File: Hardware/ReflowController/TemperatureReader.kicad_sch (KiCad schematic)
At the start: 12 parts, among them U4 MAX31865xAP

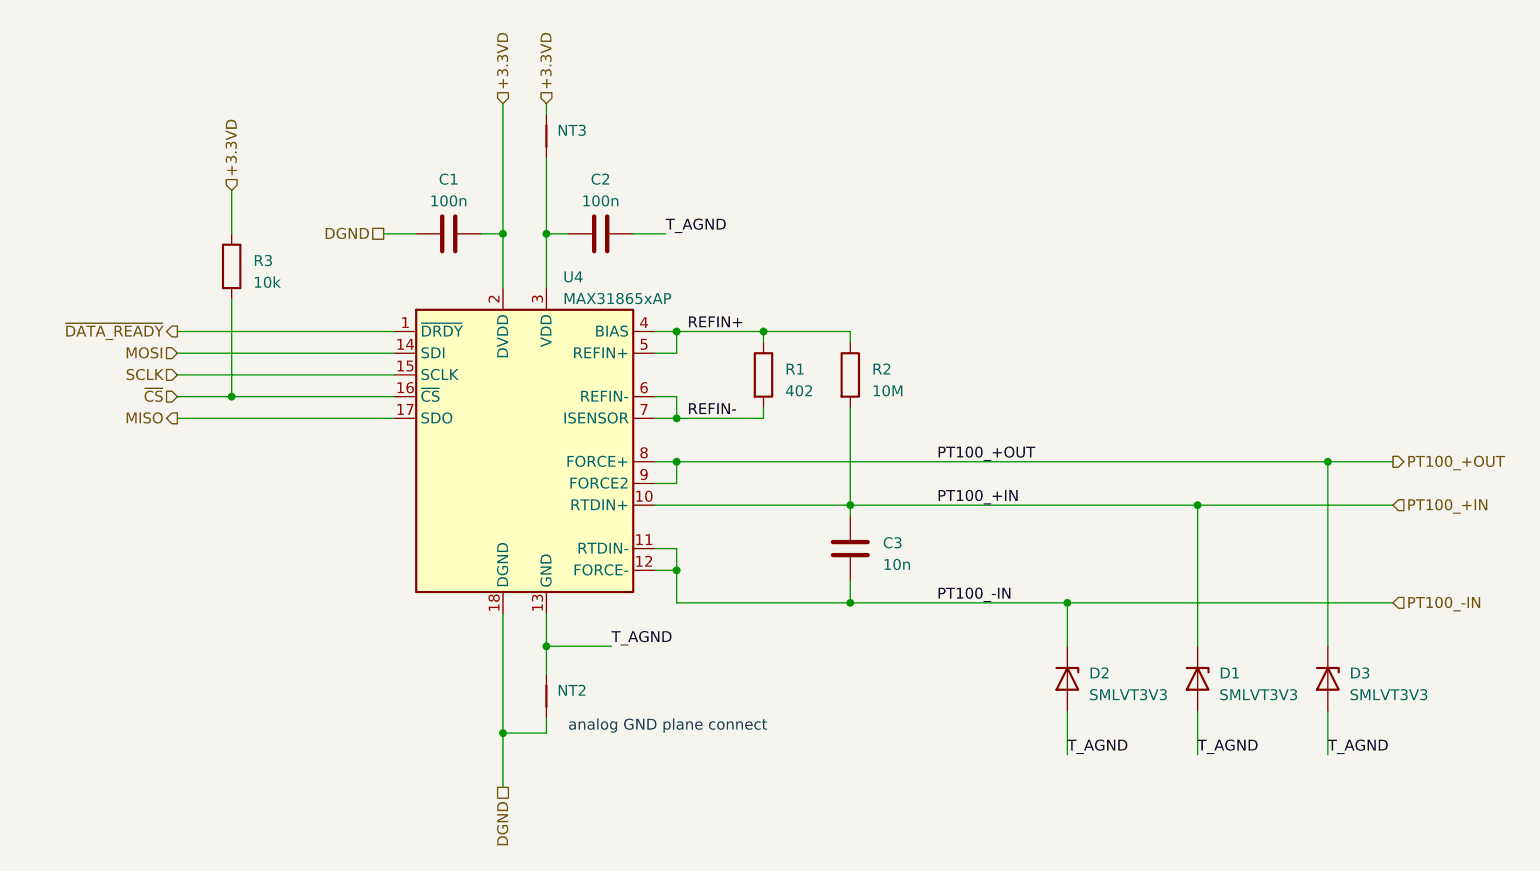
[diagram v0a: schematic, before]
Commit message: added the schematic of the updated pwerAndUi branch(with uC schematic update
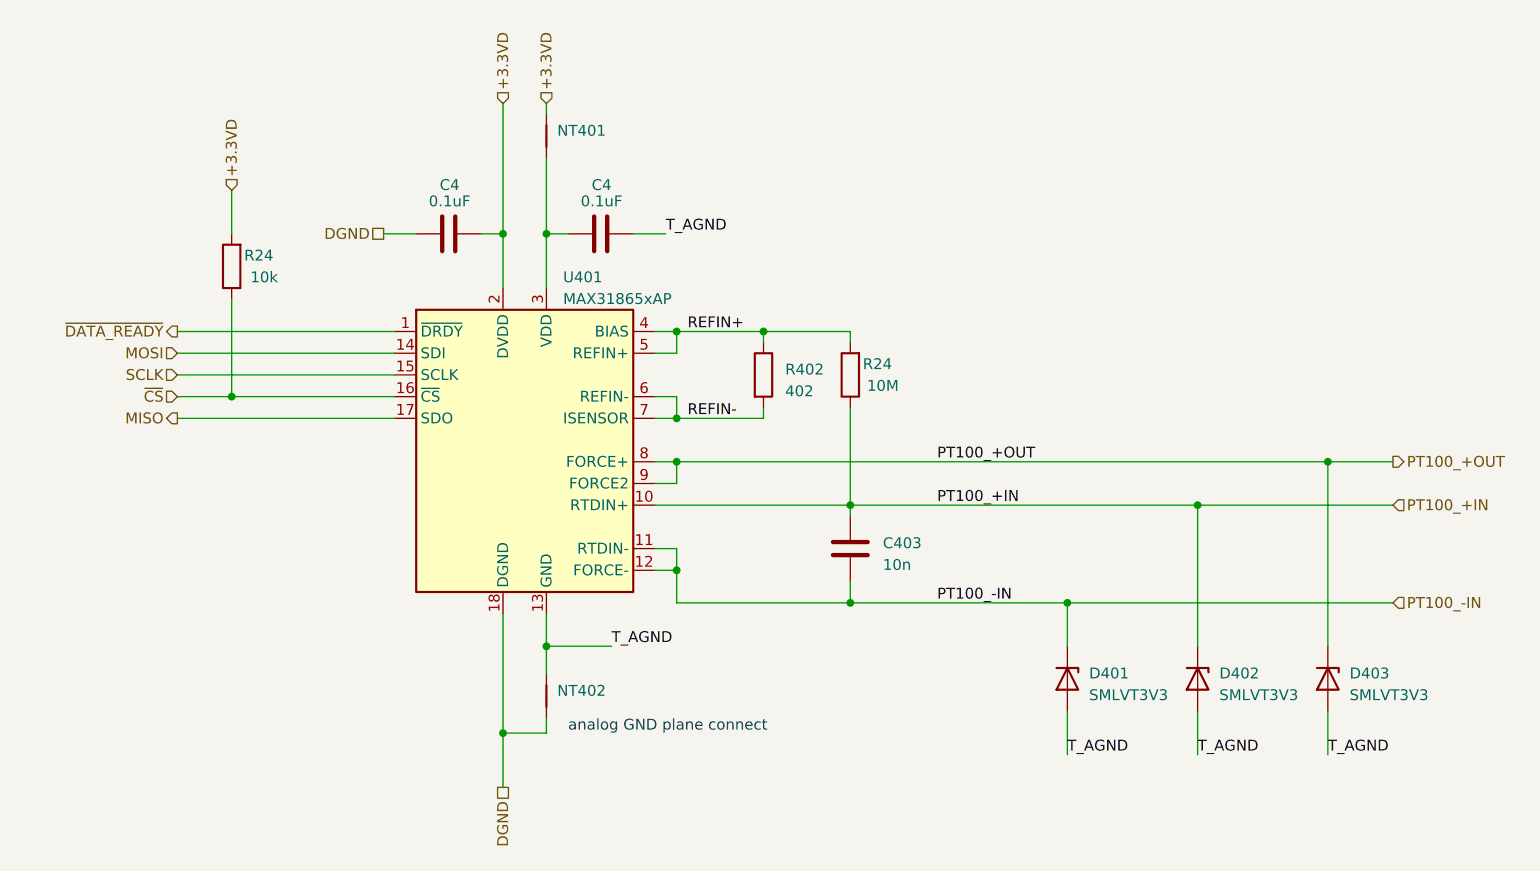
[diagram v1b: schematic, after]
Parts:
- removed C1, C2: 100n, Capacitor_SMD:C_1206_3216Metric, symbol Device:C
- removed D1, D3: SMLVT3V3, symbol Device:D_Zener
- removed R2: 10M, Resistor_SMD:R_1206_3216Metric, symbol Device:R
- removed R3: 10k, Resistor_SMD:R_1206_3216Metric, symbol Device:R
- added C4 (x2): 0.1uF, Capacitor_SMD:C_1206_3216Metric, symbol Device:C
- added D402, D403: SMLVT3V3, Diode_SMD:D_SMB_Handsoldering, symbol Device:D_Zener
- added R24: 10M, Resistor_SMD:R_0603_1608Metric_Pad0.98x0.95mm_HandSolder, symbol Device:R
- added R24: 10k, Resistor_SMD:R_0603_1608Metric_Pad0.98x0.95mm_HandSolder, symbol Device:R
- C403: renamed from C3; Field8 (none) -> 490-1754-2-ND; disti (none) -> digikey; man (none) -> murata; man_no (none) -> GRM3195C1H103JA01D
- D401: renamed from D2; footprint (none) -> Diode_SMD:D_SMB_Handsoldering; disti (none) -> digikey; disti_no (none) -> 497-2496-2-ND; man (none) -> stm; man_no (none) -> SMLVT3V3
- NT401: renamed from NT3; footprint (none) -> NetTie:NetTie-2_SMD_Pad0.5mm
- NT402: renamed from NT2; footprint (none) -> NetTie:NetTie-2_SMD_Pad0.5mm
- R402: renamed from R1; footprint (none) -> Resistor_SMD:R_1206_3216Metric; disti (none) -> digikey; disti_no (none) -> A140365TR-ND; man (none) -> te; manNo RQ73C2B402RBTD -> (none); man_no (none) -> RQ73C2B402RBTD
- renumbered U4 to U401
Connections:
- net +3.3VD: now also C4.2, R24.2
- net DGND: now also C4.1
- net PT100_+IN: now also D402.1 (K), R24.1
- net PT100_+OUT: now also D403.1 (K)
- net REFIN+: now also R24.2
- net T_AGND: now also C4.2, D402.2 (A), D403.2 (A)
- net ~{CS}: now also R24.1
- net at NT401.1, U401.3 (VDD): now also C4.1

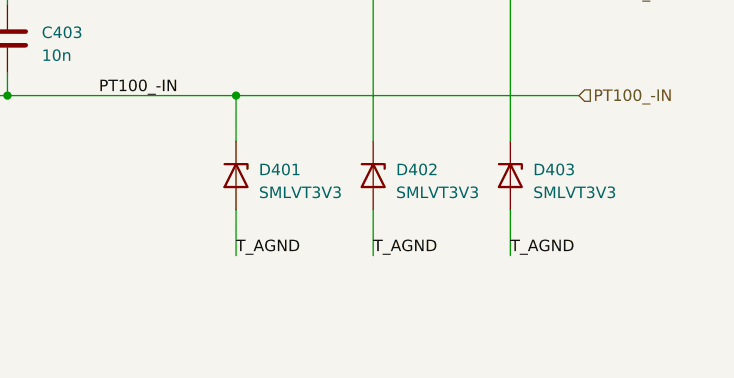
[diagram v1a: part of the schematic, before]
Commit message: work on +24V power
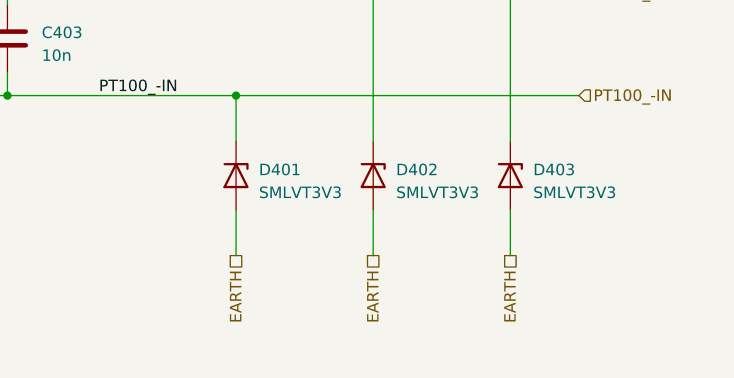
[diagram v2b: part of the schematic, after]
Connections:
- net T_AGND: no longer D401.2 (A), D402.2 (A), D403.2 (A)
- new net EARTH: D401.2 (A), D402.2 (A), D403.2 (A)
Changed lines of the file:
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@@
-    (effects (font (size 1.27 1.27)) (justify left bottom))
-  )
-  (label "T_AGND" (at 210.82 129.54 0) (fields_autoplaced)
     (effects (font (size 1.27 1.27)) (justify left bottom))
   )
@@
     (effects (font (size 1.27 1.27)) (justify left bottom))
   )
-  (label "T_AGND" (at 195.58 129.54 0) (fields_autoplaced)
-    (effects (font (size 1.27 1.27)) (justify left bottom))
-  )
   (label "PT100_+IN" (at 165.1 100.33 0) (fields_autoplaced)
-    (effects (font (size 1.27 1.27)) (justify left bottom))
-  )
-  (label "T_AGND" (at 180.34 129.54 0) (fields_autoplaced)
     (effects (font (size 1.27 1.27)) (justify left bottom))
   )
@@
     (effects (font (size 1.27 1.27)) (justify left))
   )
+  (hierarchical_label "EARTH" (shape passive) (at 180.34 129.54 270) (fields_autoplaced)
+    (effects (font (size 1.27 1.27)) (justify right))
+  )
   (hierarchical_label "PT100_+IN" (shape input) (at 218.44 100.33 0) (fields_autoplaced)
     (effects (font (size 1.27 1.27)) (justify left))
@@
     (effects (font (size 1.27 1.27)) (justify left))
   )
+  (hierarchical_label "EARTH" (shape passive) (at 195.58 129.54 270) (fields_autoplaced)
+    (effects (font (size 1.27 1.27)) (justify right))
+  )
   (hierarchical_label "SCLK" (shape input) (at 76.2 85.09 180) (fields_autoplaced)
     (effects (font (size 1.27 1.27)) (justify right))
@@
     (effects (font (size 1.27 1.27)) (justify left))
   )
+  (hierarchical_label "EARTH" (shape passive) (at 210.82 129.54 270) (fields_autoplaced)
+    (effects (font (size 1.27 1.27)) (justify right))
+  )
   (hierarchical_label "MISO" (shape output) (at 76.2 90.17 180) (fields_autoplaced)

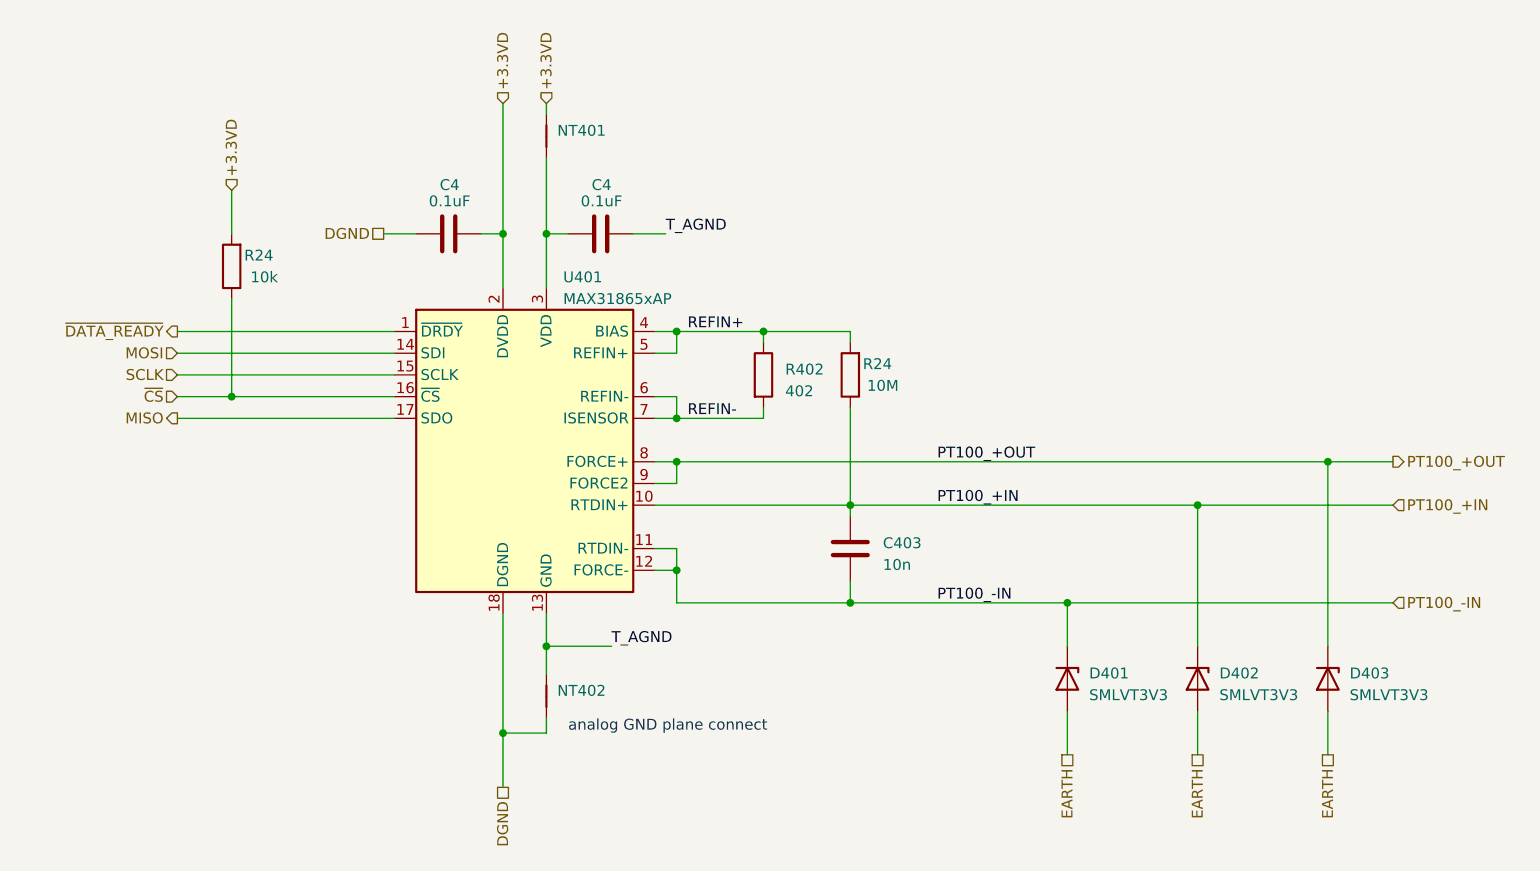
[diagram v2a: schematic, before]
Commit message: Finished rewiev with Edwin, Need TO connect he HSS and DO the labeling
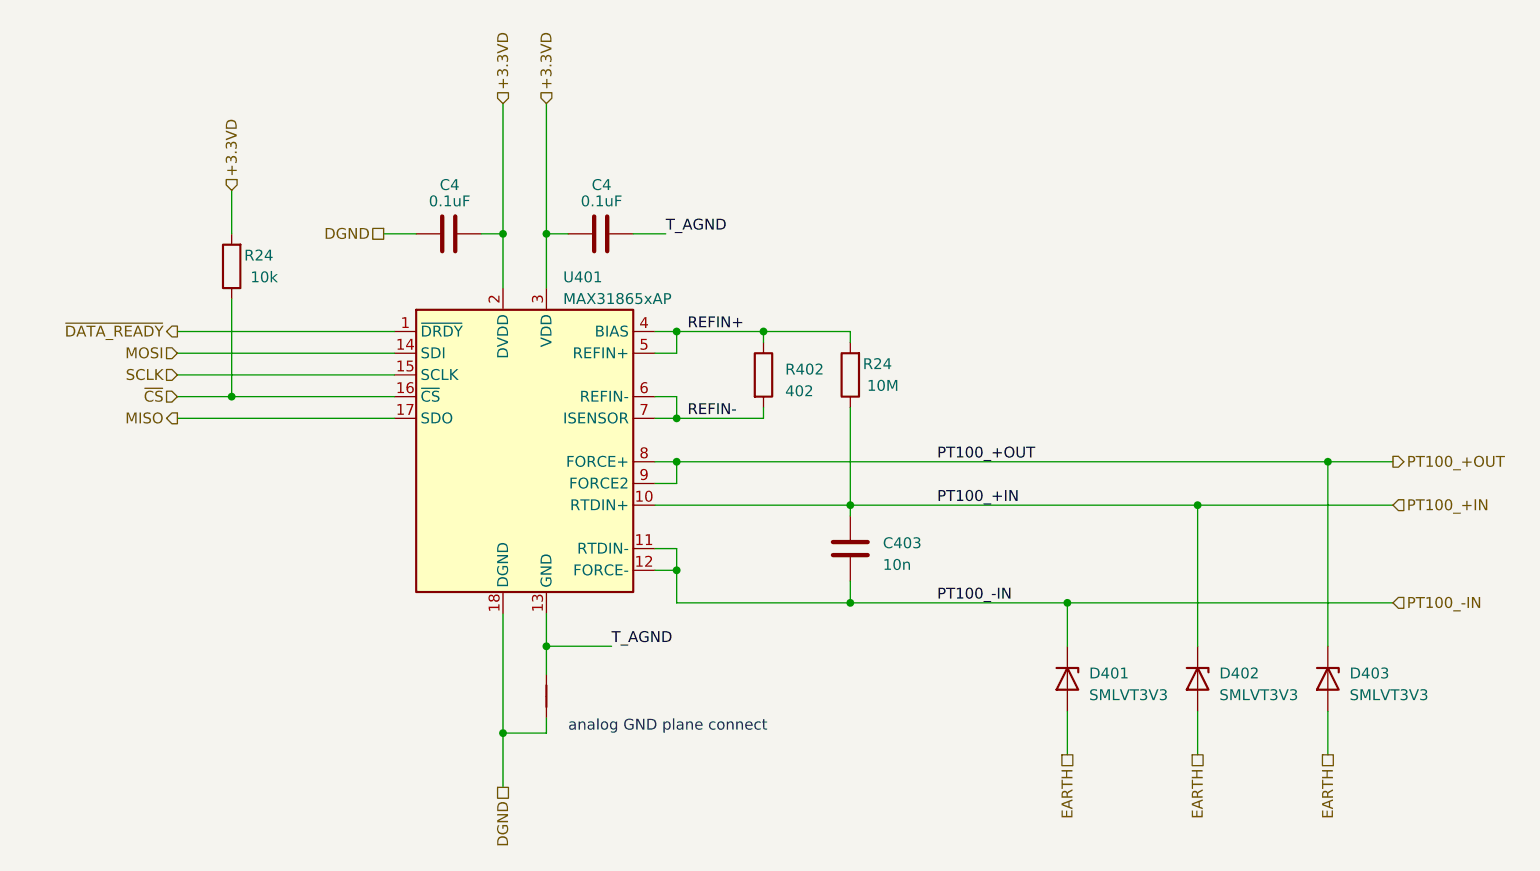
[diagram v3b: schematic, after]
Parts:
- removed NT401: NetTie_2, NetTie:NetTie-2_SMD_Pad0.5mm, symbol Device:NetTie_2
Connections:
- net +3.3VD: now also C4.1, U401.3 (VDD)
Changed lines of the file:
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@@
     (stroke (width 0) (type default))
   )
-  (wire (pts (xy 119.38 53.34) (xy 119.38 54.61))
+  (wire (pts (xy 119.38 53.34) (xy 119.38 68.58))
     (stroke (width 0) (type default))
   )
@@
   )
   (wire (pts (xy 134.62 80.01) (xy 144.78 80.01))
-    (stroke (width 0) (type default))
-  )
-  (wire (pts (xy 119.38 59.69) (xy 119.38 68.58))
     (stroke (width 0) (type default))
   )
@@
     )
   )
-  (symbol (lib_id "Device:NetTie_2") (at 119.38 57.15 90) (unit 1)
-    (in_bom no) (on_board yes) (dnp no) (fields_autoplaced)
-    (property "Reference" "NT401" (at 120.65 56.515 90)
-      (effects (font (size 1.27 1.27)) (justify right))
-    )
-    (property "Value" "NetTie_2" (at 120.65 59.055 90)
-      (effects (font (size 1.27 1.27)) (justify right) hide)
-    )
-    (property "Footprint" "NetTie:NetTie-2_SMD_Pad0.5mm" (at 119.38 57.15 0)
-      (effects (font (size 1.27 1.27)) hide)
-    )
-    (property "Datasheet" "~" (at 119.38 57.15 0)
-      (effects (font (size 1.27 1.27)) hide)
-    )
-    (pin "1")
-    (pin "2")
-    (instances
-      (project "ReflowController"
-        (path "/2394cc2a-b9b0-4c0b-be11-1fc6085b0d5c/cedd135a-27b6-4ce6-9f5e-bdcd93291ccf"
-          (reference "NT401") (unit 1)
-        )
-      )
-    )
-  )
   (symbol (lib_id "Device:R") (at 82.55 72.39 180) (unit 1)
     (in_bom yes) (on_board yes) (dnp no)
@@
     (in_bom no) (on_board yes) (dnp no) (fields_autoplaced)
     (property "Reference" "NT402" (at 120.65 122.047 90)
-      (effects (font (size 1.27 1.27)) (justify right))
+      (effects (font (size 1.27 1.27)) (justify right) hide)
     )
     (property "Value" "NetTie_2" (at 120.65 124.587 90)

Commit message: work on BOM cleanup
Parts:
- C403: Field8 490-1754-2-ND -> (none); disti_no (none) -> 490-1754-2-ND
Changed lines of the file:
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@@
       (effects (font (size 1.27 1.27)) hide)
     )
-    (property "Field8" "490-1754-2-ND" (at 154.94 105.41 0)
+    (property "Field8" "" (at 154.94 105.41 0)
       (effects (font (size 1.27 1.27)) hide)
     )
+    (property "disti_no" "490-1754-2-ND" (at 154.94 105.41 0)
+      (effects (font (size 1.27 1.27)) hide)
+    )
